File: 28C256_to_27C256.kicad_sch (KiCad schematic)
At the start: 4 parts, among them J1 27C256 DIP LEGS, U1 28C256

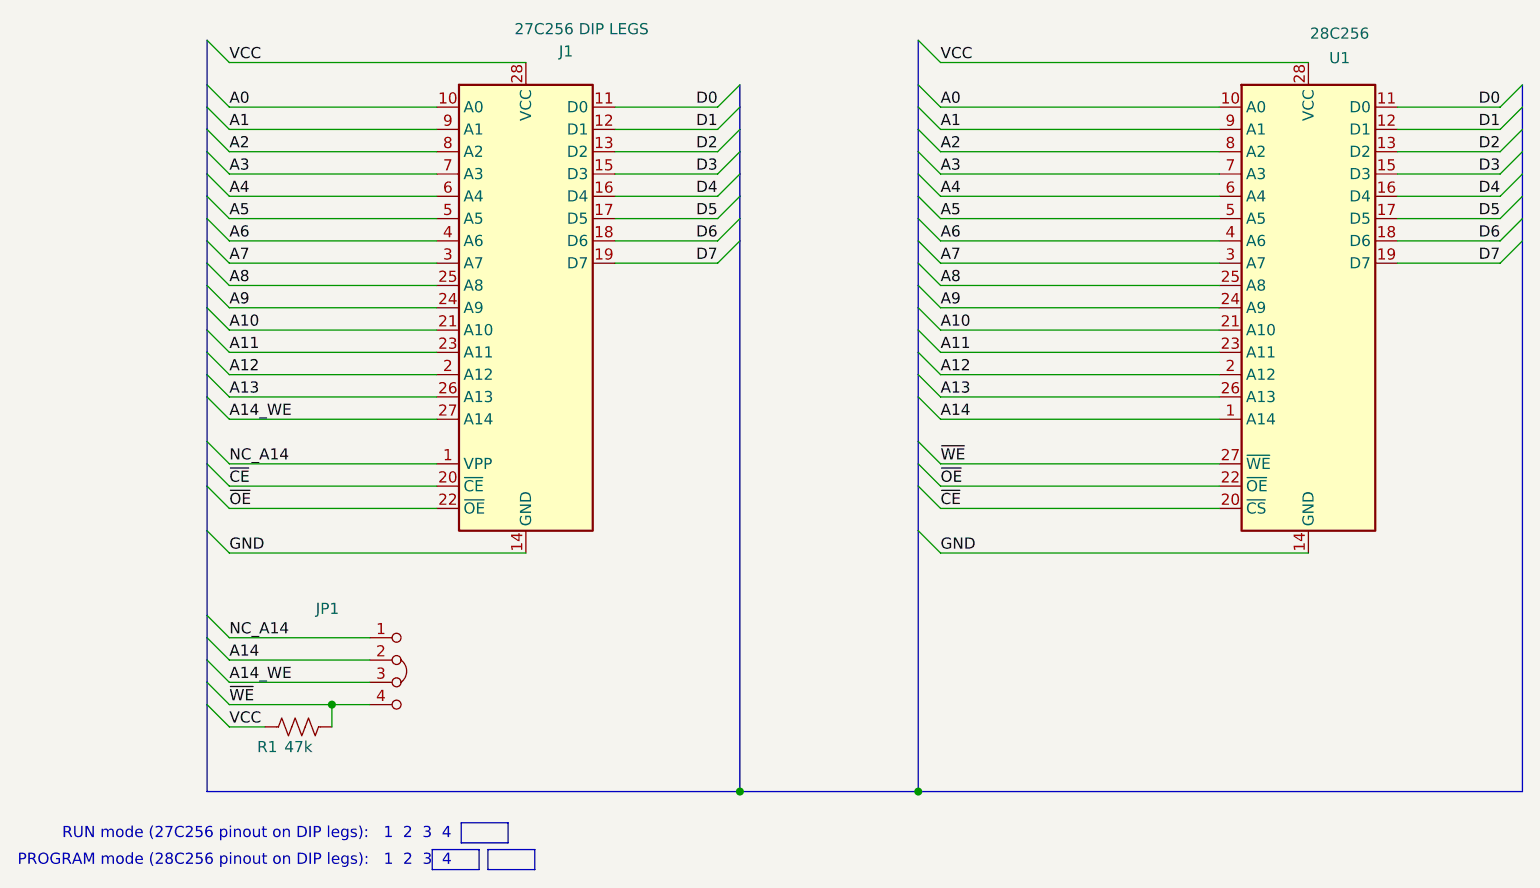
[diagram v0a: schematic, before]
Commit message: Fix wrong pinout on FlashROM_100 TSOPgit add -A!
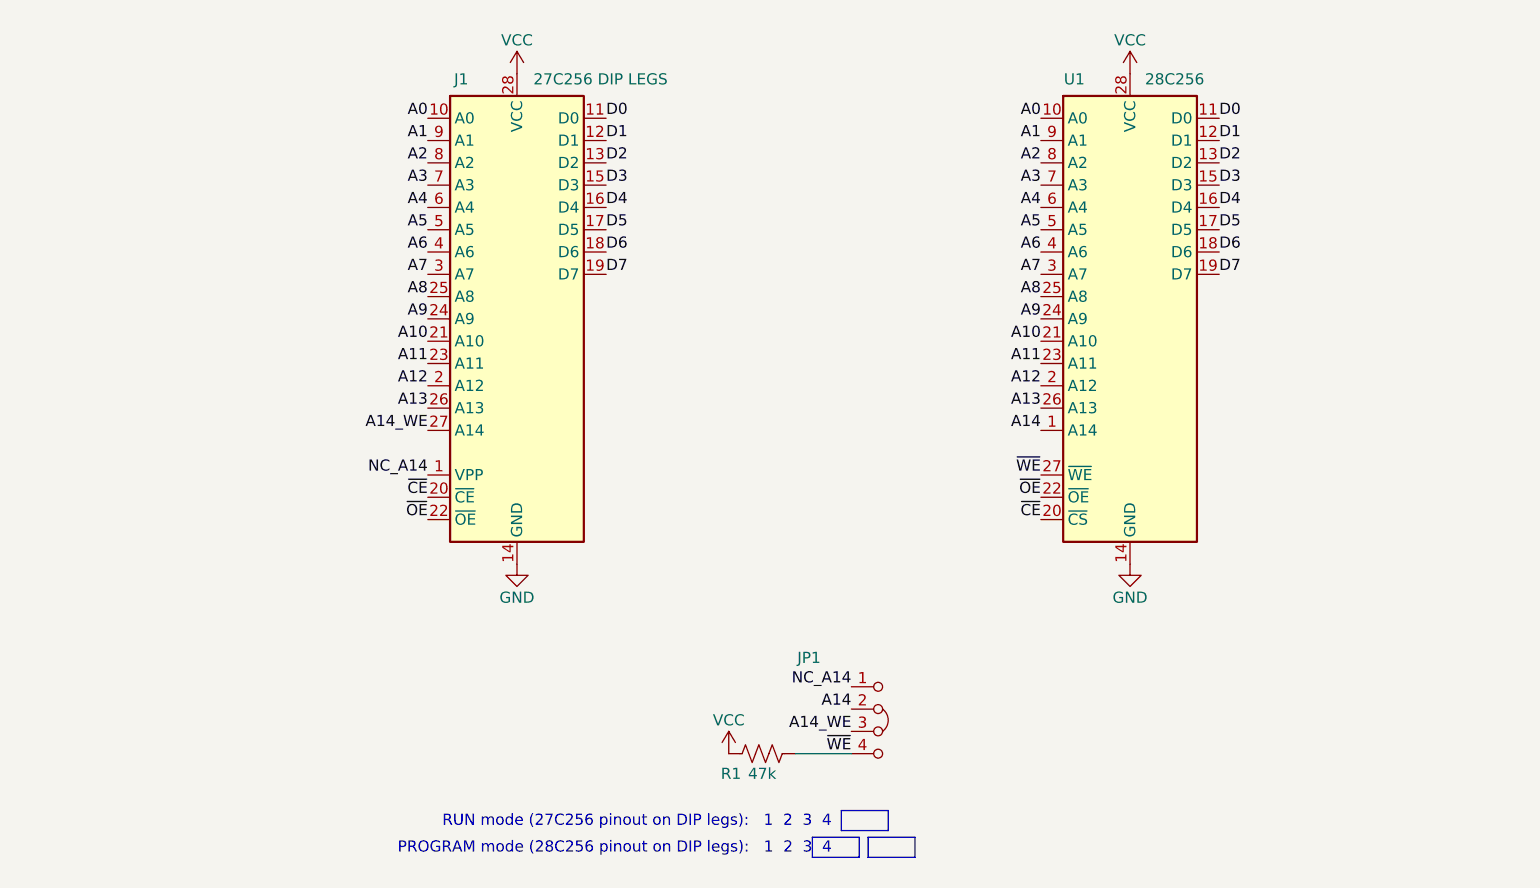
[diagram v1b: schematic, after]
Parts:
- J1: footprint 000_LOCAL:DIP28_0.6_pcb_sil_pins -> 000_LOCAL:DIP28_0.6_pcb
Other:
- moved on the sheet: J1, JP1, R1, U1
